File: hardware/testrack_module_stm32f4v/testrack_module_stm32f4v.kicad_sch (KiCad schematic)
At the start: 22 parts, among them J1 Bus_M.2_Socket_B, U1 STM32F407VGTx, U2 LT1962-3.3, U3 24AA01-I/SN, Y1 32.768kHz, Y2 12MHz

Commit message: Laid out and routed the testrack_module_stm32f4v board
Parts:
- Y1: footprint (none) -> rhais_osc:SMD3215
- Y2: symbol Device:Crystal -> Device:Crystal_GND24
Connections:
- net GND: now also Y2.2, Y2.4
- net GPIO0: now also J1.20 (GPIO_5); no longer J1.40 (GPIO_0)
- net GPIO1: now also J1.22 (GPIO_6); no longer J1.42 (GPIO_1)
- net GPIO2: now also J1.24 (GPIO_7); no longer J1.44 (GPIO_2)
- net GPIO3: now also J1.48 (GPIO_4); no longer J1.46 (GPIO_3)
- net GPIO4: now also J1.46 (GPIO_3); no longer J1.48 (GPIO_4)
- net GPIO5: now also J1.44 (GPIO_2); no longer J1.20 (GPIO_5)
- net GPIO6: now also J1.42 (GPIO_1); no longer J1.22 (GPIO_6)
- net GPIO7: now also J1.40 (GPIO_0); no longer J1.24 (GPIO_7)
- net JTCK: now also J1.32 (UIM-CLK); no longer J1.34 (UIM-DATA)
- net JTDI: now also J1.34 (UIM-DATA); no longer J1.32 (UIM-CLK)
- net JTDO: now also J1.36 (UIM-PWR); no longer J1.30 (UIM-RESET)
- net JTMS: now also J1.30 (UIM-RESET); no longer J1.36 (UIM-PWR)
- net TRACECLK: now also J1.69 (CONFIG_1); no longer J1.59 (ANTCTL0)
- net TRACED0: now also J1.67 (~{RESET}); no longer J1.1 (CONFIG_3)
- net TRACED1: now also J1.65 (ANTCTL3); no longer J1.75 (CONFIG_2)
- net TRACED2: now also J1.63 (ANTCTL2); no longer J1.69 (CONFIG_1)
- net TRACED3: now also J1.61 (ANTCTL1); no longer J1.21 (CONFIG_0)
- net at C9.1, U1.12 (PH0): now also Y2.3; no longer Y2.2
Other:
- moved on the sheet: U3

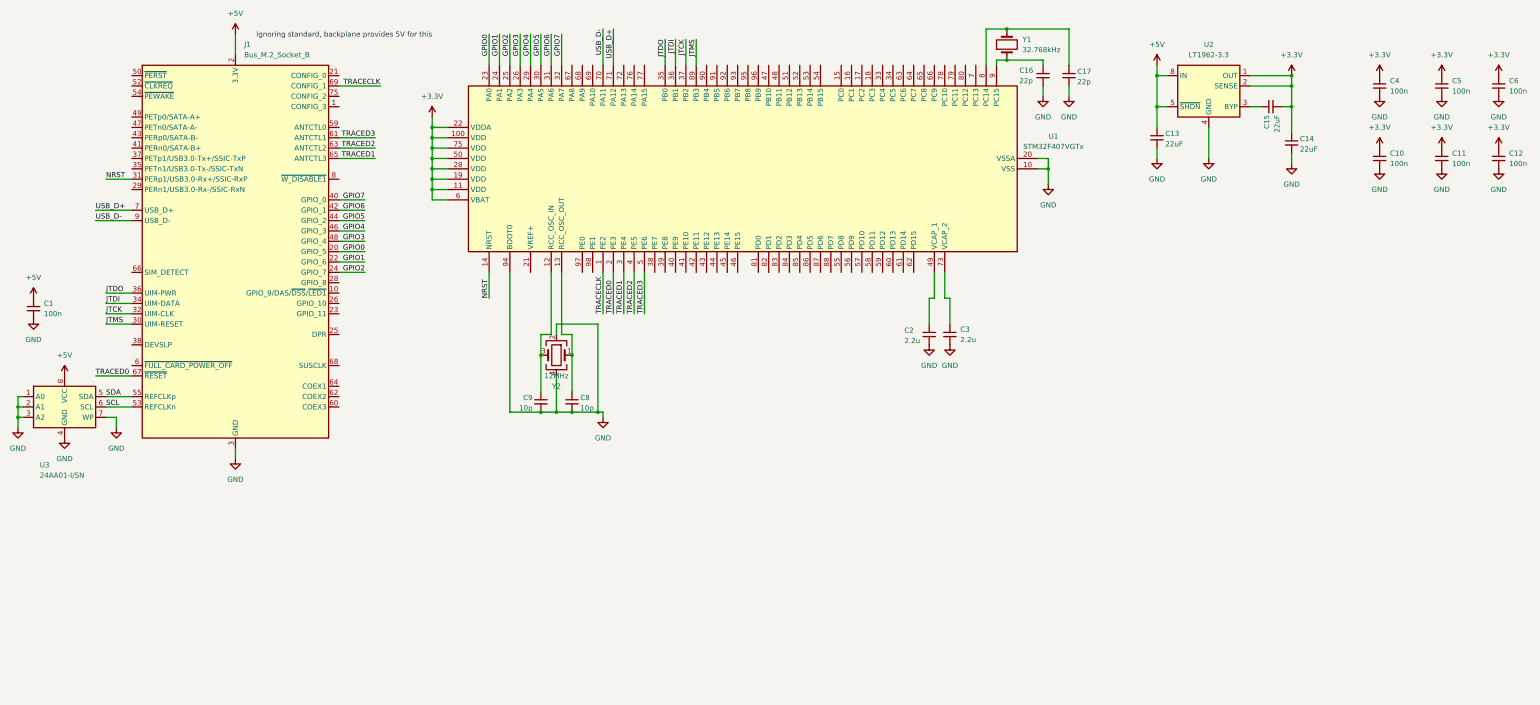
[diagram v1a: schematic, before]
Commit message: switching the connector over to the new custom symbol and tied up loose ends
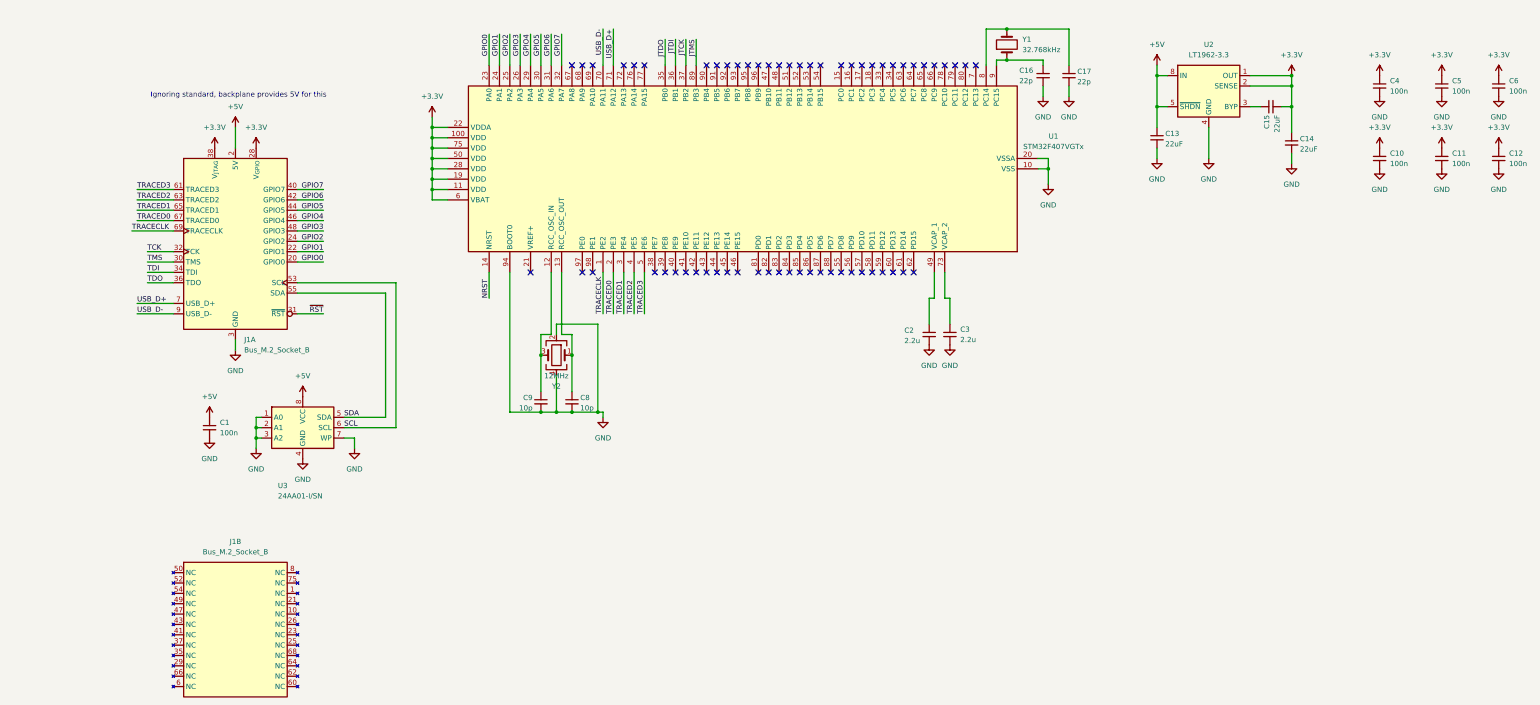
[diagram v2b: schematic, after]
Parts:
- J1: symbol Connector:Bus_M.2_Socket_B -> redcuttle_testrack:redcuttle-testrack-module-cardedge
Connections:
- net +3.3V: now also J1.28 (V_{GPIO}), J1.38 (V_{JTAG})
- net JTCK: no longer J1.32 (UIM-CLK)
- net JTDI: no longer J1.34 (UIM-DATA)
- net JTDO: no longer J1.36 (UIM-PWR)
- net JTMS: no longer J1.30 (UIM-RESET)
- net NRST: no longer J1.31 (PERp1/USB3.0-Rx+/SSIC-RxP)
- new net TCK: J1.32 (TCK)
- new net TDI: J1.34 (TDI)
- new net TDO: J1.36 (TDO)
- new net TMS: J1.30 (TMS)
- new net ~{RST}: J1.31 (~{RST})
- no-connect marks 0 -> 60
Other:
- moved on the sheet: C1, U3

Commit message: Added the mounting hole to the target board
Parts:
- added H1: MountingHole_Pad, MountingHole:MountingHole_2.7mm_M2.5_Pad, symbol Mechanical:MountingHole_Pad
- added unit 1 of J1
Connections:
- net +3.3V: now also J1.28 (V_{GPIO}), J1.38 (V_{JTAG}); no longer J1.28 (V_{GPIO}), J1.38 (V_{JTAG})
- net +5V: now also J1.2 (5V), J1.4 (5V), J1.70 (5V), J1.72 (5V), J1.74 (5V); no longer J1.2 (5V), J1.4 (5V), J1.70 (5V), J1.72 (5V), J1.74 (5V)
- net GND: now also H1.1, J1.11 (GND), J1.27 (GND), J1.3 (GND), J1.33 (GND), J1.39 (GND), J1.45 (GND), J1.5 (GND), J1.51 (GND), J1.57 (GND), J1.71 (GND), J1.73 (GND); no longer J1.11 (GND), J1.27 (GND), J1.3 (GND), J1.33 (GND), J1.39 (GND), J1.45 (GND), J1.5 (GND), J1.51 (GND), J1.57 (GND), J1.71 (GND), J1.73 (GND)
- net GPIO0: now also J1.20 (GPIO0); no longer J1.20 (GPIO0)
- net GPIO1: now also J1.22 (GPIO1); no longer J1.22 (GPIO1)
- net GPIO2: now also J1.24 (GPIO2); no longer J1.24 (GPIO2)
- net GPIO3: now also J1.48 (GPIO3); no longer J1.48 (GPIO3)
- net GPIO4: now also J1.46 (GPIO4); no longer J1.46 (GPIO4)
- net GPIO5: now also J1.44 (GPIO5); no longer J1.44 (GPIO5)
- net GPIO6: now also J1.42 (GPIO6); no longer J1.42 (GPIO6)
- net GPIO7: now also J1.40 (GPIO7); no longer J1.40 (GPIO7)
- net SCL: now also J1.53 (SCL); no longer J1.53 (SCL)
- net SDA: now also J1.55 (SDA); no longer J1.55 (SDA)
- net TCK: now also J1.32 (TCK); no longer J1.32 (TCK)
- net TDI: now also J1.34 (TDI); no longer J1.34 (TDI)
- net TDO: now also J1.36 (TDO); no longer J1.36 (TDO)
- net TMS: now also J1.30 (TMS); no longer J1.30 (TMS)
- net TRACECLK: now also J1.69 (TRACECLK); no longer J1.69 (TRACECLK)
- net TRACED0: now also J1.67 (TRACED0); no longer J1.67 (TRACED0)
- net TRACED1: now also J1.65 (TRACED1); no longer J1.65 (TRACED1)
- net TRACED2: now also J1.63 (TRACED2); no longer J1.63 (TRACED2)
- net TRACED3: now also J1.61 (TRACED3); no longer J1.61 (TRACED3)
- net USB_D+: now also J1.7 (USB_D+); no longer J1.7 (USB_D+)
- net USB_D-: now also J1.9 (USB_D-); no longer J1.9 (USB_D-)
- net ~{RST}: now also J1.31 (~{RST}); no longer J1.31 (~{RST})
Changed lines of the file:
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@@
+	(symbol
+		(lib_id "power:GND")
+		(at 119.38 161.29 0)
+		(unit 1)
+		(exclude_from_sim no)
+		(in_bom yes)
+		(on_board yes)
+		(dnp no)
+		(fields_autoplaced yes)
+		(property "Reference" "#PWR035"
+			(at 119.38 167.64 0)
+			(effects
+				(font
+					(size 1.27 1.27)
+				)
+				(hide yes)
+			)
+		)
+		(property "Value" "GND"
+			(at 119.38 166.37 0)
+			(effects
+				(font
+					(size 1.27 1.27)
+				)
+			)
+		)
+		(property "Footprint" ""
+			(at 119.38 161.29 0)
+			(effects
+				(font
+					(size 1.27 1.27)
+				)
+				(hide yes)
+			)
+		)
+		(property "Datasheet" ""
+			(at 119.38 161.29 0)
+			(effects
+				(font
+					(size 1.27 1.27)
+				)
+				(hide yes)
+			)
+		)
+		(property "Description" "Power symbol creates a global label with name \"GND\" , ground"
+			(at 119.38 161.29 0)
+			(effects
+				(font
+					(size 1.27 1.27)
+				)
+				(hide yes)
+			)
+		)
+		(pin "1"
+		)
+		(instances
+			(project ""
+				(path "/f21efc02-04a9-43dd-a97e-db9f6d578424"
+					(reference "#PWR035")
+					(unit 1)
+				)
+			)
+		)
+	)
 	(symbol
 		(lib_id "power:GND")
@@
 					(unit 1)
 				)
+			)
+		)
+	)
+	(symbol
+		(lib_id "Mechanical:MountingHole_Pad")
+		(at 119.38 158.75 0)
+		(unit 1)
+		(exclude_from_sim no)
+		(in_bom no)
+		(on_board yes)
+		(dnp no)
+		(fields_autoplaced yes)
+		(property "Reference" "H1"
+			(at 121.92 156.2099 0)
+			(effects
+				(font
+					(size 1.27 1.27)
+				)
+				(justify left)
+			)
+		)
+		(property "Value" "MountingHole_Pad"
+			(at 121.92 158.7499 0)
+			(effects
+				(font
+					(size 1.27 1.27)
+				)
+				(justify left)
+			)
+		)
+		(property "Footprint" "MountingHole:MountingHole_2.7mm_M2.5_Pad"
+			(at 119.38 158.75 0)
+			(effects
+				(font
+					(size 1.27 1.27)
+				)
+				(hide yes)
+			)
+		)
+		(property "Datasheet" "~"
+			(at 119.38 158.75 0)
+			(effects
+				(font
+					(size 1.27 1.27)
+				)
+				(hide yes)
+			)
+		)
+		(property "Description" "Mounting Hole with connection"
+			(at 119.38 158.75 0)
+			(effects
+				(font
+					(size 1.27 1.27)
+				)
+				(hide yes)
+			)
+		)
+		(pin "1"
+		)
+		(instances
+			(project ""
+				(path "/f21efc02-04a9-43dd-a97e-db9f6d578424"
+					(reference "H1")
+					(unit 1)
+				)
